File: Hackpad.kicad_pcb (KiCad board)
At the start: 2 copper layers, 99 x 70 mm, 14 parts, among them SW1 SW_Push, SW2 SW_Push, SW3 SW_Push, SW4 SW_Push, SW5 SW_Push, SW6 RotaryEncoder_Switch_MP, U1 XIAO-RP2040-DIP

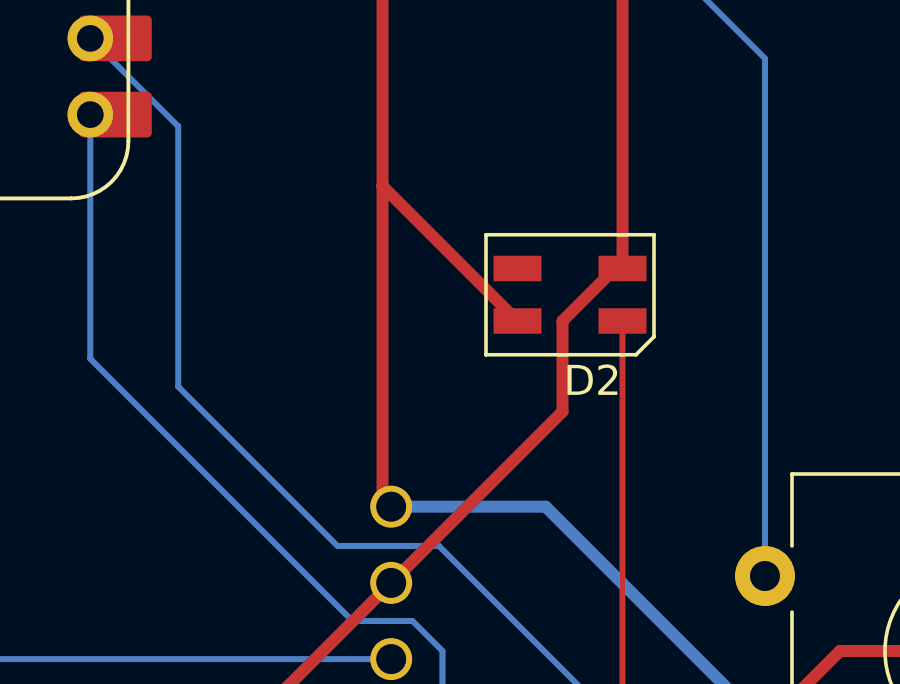
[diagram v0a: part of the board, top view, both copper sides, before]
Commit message: Reroute D2 ground
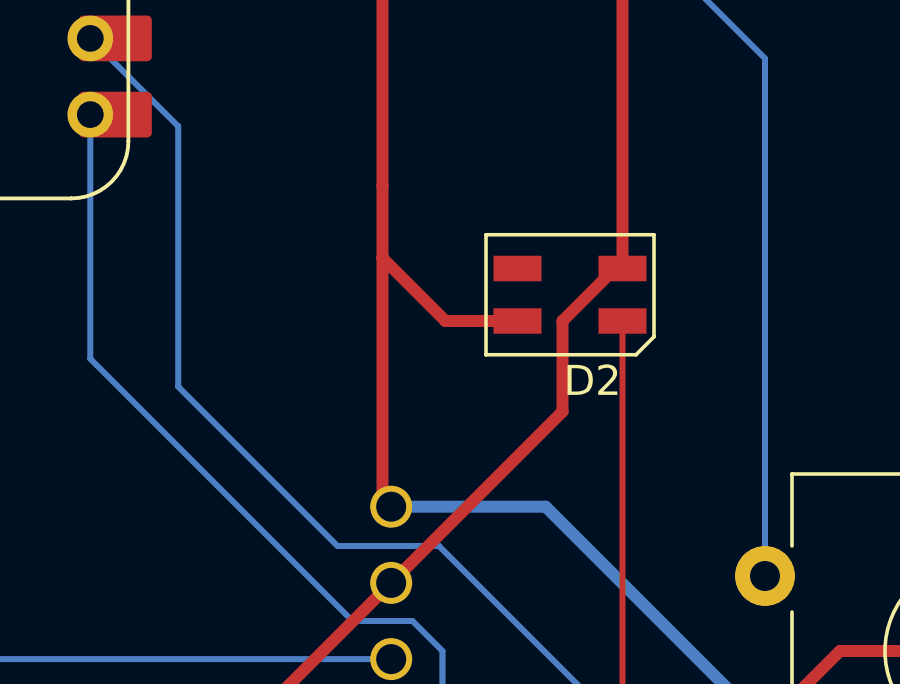
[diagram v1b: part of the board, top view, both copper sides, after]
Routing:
- net GND: track 181.7 -> 180.7 mm
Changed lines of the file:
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@@
+	)
+	(segment
+		(start 134.1 93)
+		(end 132 90.9)
+		(width 0.4)
+		(layer "F.Cu")
+		(net 5)
 	)
 	(segment
@@
 	)
 	(segment
-		(start 132 88.5)
+		(start 132 90.9)
 		(end 132 98.9)
 		(width 0.4)
@@
 		(start 145.415 121.12625)
 		(end 107.315 121.12625)
+		(width 0.4)
+		(layer "F.Cu")
+		(net 5)
+	)
+	(segment
+		(start 136.5 93)
+		(end 134.1 93)
 		(width 0.4)
 		(layer "F.Cu")
@@
 	(segment
 		(start 132 88.5)
-		(end 136.5 93)
+		(end 132 90.9)
 		(width 0.4)
 		(layer "F.Cu")

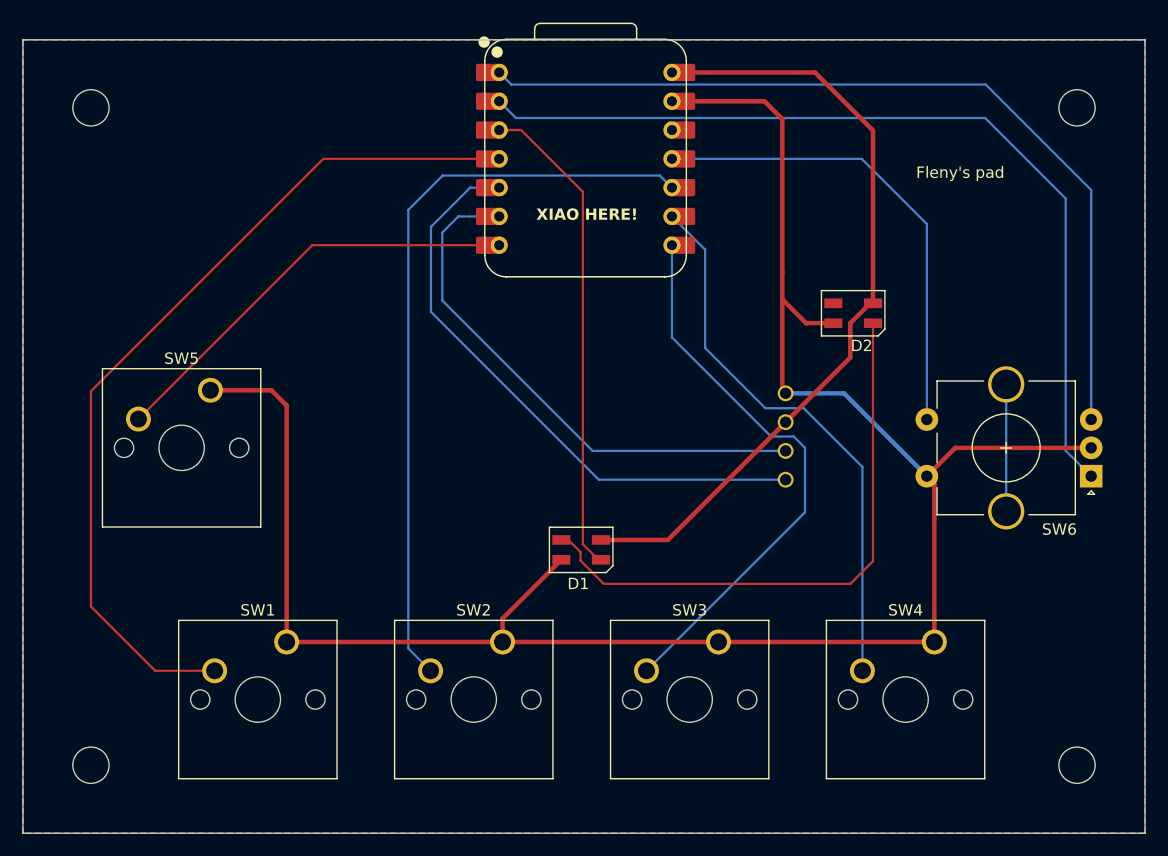
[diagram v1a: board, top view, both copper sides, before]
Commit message: Resize routes
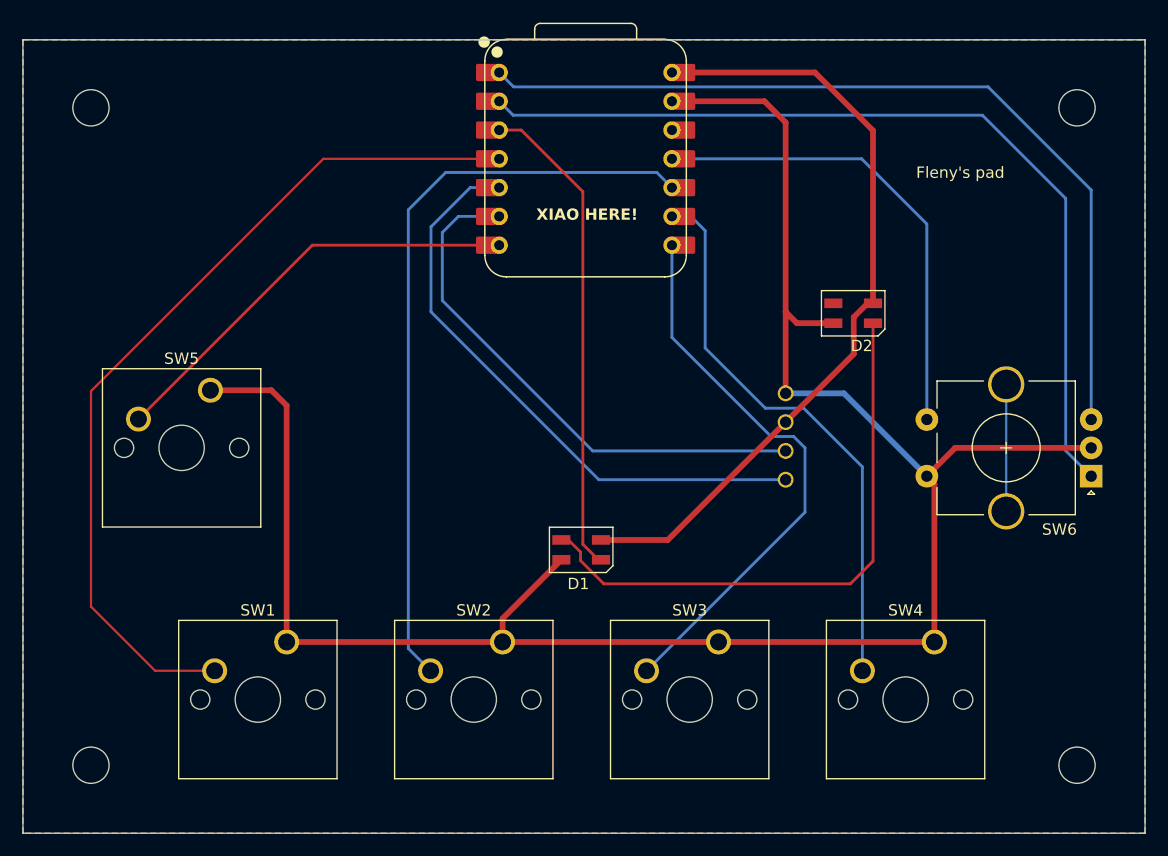
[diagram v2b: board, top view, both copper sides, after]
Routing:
- net Net-(U1-GPIO2/SCK): track 49.0 -> 50.0 mm
- net GND: track 180.7 -> 179.9 mm
- net Net-(D1-DOUT): track 51.4 -> 50.7 mm

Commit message: Rotate oled & reroute
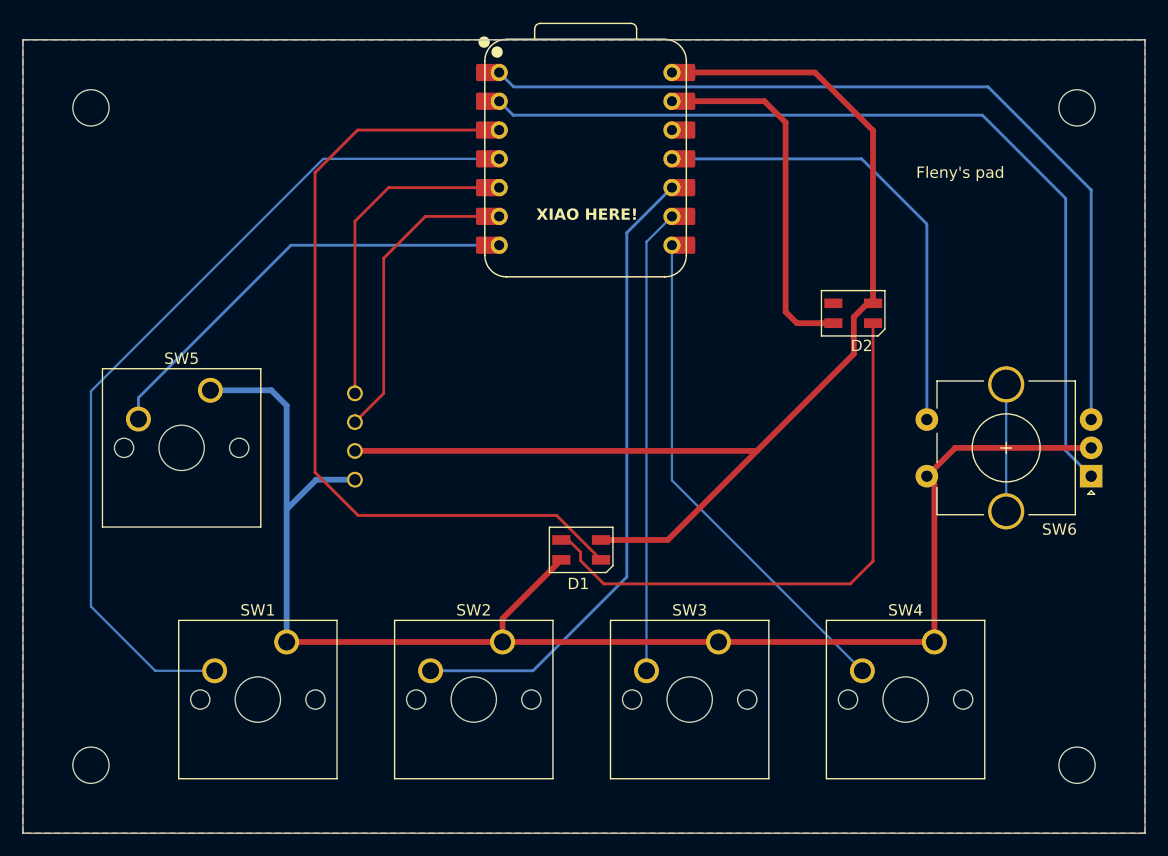
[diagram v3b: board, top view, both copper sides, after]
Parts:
- moved OL1 38.0 mm to (94.3, 103.0), turned to -90 degrees
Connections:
- SW3 pad 2: Net-(U1-GPIO1/RX) -> Net-(U1-GPIO2/SCK)
- SW4 pad 2: Net-(U1-GPIO2/SCK) -> Net-(U1-GPIO1/RX)
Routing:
- net +5V: track 69.2 -> 104.6 mm
- net Net-(D1-DIN): track 42.7 -> 72.7 mm
- net Net-(OL1-SDA): track 52.4 -> 29.1 mm
- net Net-(OL1-SCL): track 47.4 -> 27.2 mm
- net GND: track 179.9 -> 164.4 mm
- net Net-(U1-GPIO4/MISO): track 66.7 -> 56.7 mm
- net Net-(U1-GPIO2/SCK): track 50.0 -> 41.0 mm
- net Net-(U1-GPIO1/RX): track 49.4 -> 44.5 mm
- net Net-(U1-GPIO0/TX): track 38.2 -> 39.3 mm

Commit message: Center oled, SW5 and Rotary
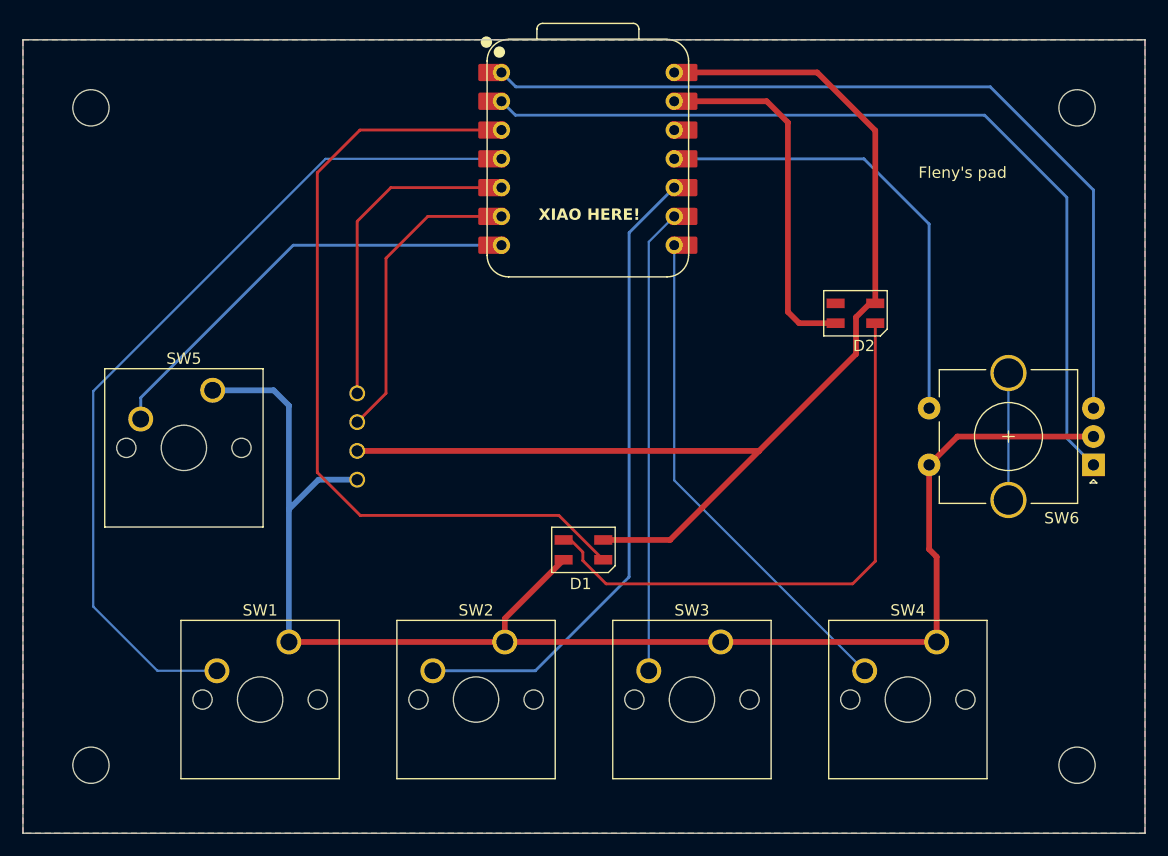
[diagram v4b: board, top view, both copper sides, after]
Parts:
- moved SW6 1.02 mm to (159.4, 105.5)
- moved SW4 0.20 mm to (145.6, 121.1)
- moved D1 0.20 mm to (114.5, 113.0)
- moved SW1 0.20 mm to (88.5, 121.1)
- moved SW2 0.20 mm to (107.5, 121.1)
- moved SW3 0.20 mm to (126.6, 121.1)
- moved U1 0.20 mm to (114.8, 78.5)
- moved D2 0.20 mm to (138.4, 92.1)
- moved OL1 0.20 mm to (94.5, 103.0)
- moved SW5 0.20 mm to (81.7, 98.9)
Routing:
- net GND: track 164.4 -> 165.4 mm
- net Net-(U1-GPIO27/ADC1/A1): track 79.0 -> 78.0 mm
- net Net-(U1-GPIO26/ADC0/A0): track 76.8 -> 75.8 mm
- net Net-(U1-GPIO3/MOSI): track 42.1 -> 41.1 mm

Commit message: Center
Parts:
- moved SW6 2.45 mm to (157.0, 105.5)
- moved OL1 1.26 mm to (95.8, 103.0)
- moved SW5 1.04 mm to (82.0, 97.9)
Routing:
- net GND: track 165.4 -> 167.8 mm
- net Net-(U1-GPIO0/TX): track 39.3 -> 37.5 mm
- net +5V: track 104.6 -> 103.4 mm
- net Net-(U1-GPIO27/ADC1/A1): track 78.0 -> 76.8 mm
- net Net-(U1-GPIO3/MOSI): track 41.1 -> 40.1 mm
- net Net-(U1-GPIO26/ADC0/A0): track 75.8 -> 74.8 mm
- net Net-(OL1-SDA): track 29.1 -> 29.7 mm
- net Net-(OL1-SCL): track 27.2 -> 26.7 mm
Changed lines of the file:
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@@
 	(footprint "Rotary_Encoder:RotaryEncoder_Alps_EC11E-Switch_Vertical_H20mm_CircularMountingHoles"
 		(layer "F.Cu")
-		(at 159.45 105.5 180)
+		(at 157 105.5 180)
 		(descr "Alps rotary encoder, EC12E... with switch, vertical shaft, mounting holes with circular drills, http://www.alps.com/prod/info/E/HTML/Encoder/Incremental/EC11/EC11E15204A3.html")
 		(tags "rotary encoder")
@@
 	(footprint "KBD:OLED"
 		(layer "F.Cu")
-		(at 94.49 103 -90)
+		(at 95.75 103 -90)
 		(descr "Connecteur 6 pins")
 		(tags "CONN DEV")
@@
 	(footprint "Button_Switch_Keyboard:SW_Cherry_MX_1.00u_PCB"
 		(layer "F.Cu")
-		(at 81.74 98.92)
+		(at 82.04 97.92)
 		(descr "Cherry MX keyswitch, 1.00u, PCB mount, http://cherryamericas.com/wp-content/uploads/2014/12/mx_cat.pdf")
 		(tags "Cherry MX keyswitch 1.00u PCB")
@@
 			(keep_text_aligned yes)
 		)
-		(gr_text "99"
+		(gr_text "3897.6378"
 			(at 114.5 141.85 0)
 			(layer "User.4")
@@
 			(keep_text_aligned yes)
 		)
-		(gr_text "70"
+		(gr_text "2755.9055"
 			(at 57.85 103 90)
 			(layer "User.4")
@@
 	)
 	(segment
-		(start 94.49 104.27)
+		(start 95.75 104.27)
 		(end 129.95 104.27)
 		(width 0.508)
@@
 	)
 	(segment
-		(start 94.49 84.01)
-		(end 94.49 99.19)
+		(start 97.46 81.04)
+		(end 94.49 84.01)
 		(width 0.254)
 		(layer "F.Cu")
@@
 	)
 	(segment
-		(start 97.46 81.04)
+		(start 94.49 97.93)
 		(end 94.49 84.01)
 		(width 0.254)
@@
 	)
 	(segment
+		(start 95.75 99.19)
+		(end 94.49 97.93)
+		(width 0.254)
+		(layer "F.Cu")
+		(net 2)
+	)
+	(segment
 		(start 97.03 87.27)
-		(end 97.03 99.19)
+		(end 97.03 100.45)
 		(width 0.254)
 		(layer "F.Cu")
@@
 	)
 	(segment
-		(start 97.03 99.19)
-		(end 94.49 101.73)
+		(start 95.75 101.73)
+		(end 97.03 100.45)
 		(width 0.254)
 		(layer "F.Cu")
@@
 	)
 	(segment
+		(start 145 103)
+		(end 157 103)
+		(width 0.508)
+		(layer "F.Cu")
+		(net 5)
+	)
+	(segment
 		(start 133.49 93)
 		(end 132.49 92)
@@
 	)
 	(segment
-		(start 145.615 121.12625)
-		(end 107.515 121.12625)
+		(start 142.5 105.5)
+		(end 145 103)
 		(width 0.508)
 		(layer "F.Cu")
@@
 	)
 	(segment
-		(start 147.45 103)
-		(end 159.45 103)
-		(width 0.508)
-		(layer "F.Cu")
-		(net 5)
-	)
-	(segment
-		(start 145.615 113.615)
-		(end 144.95 112.95)
-		(width 0.508)
-		(layer "F.Cu")
-		(net 5)
-	)
-	(segment
-		(start 144.95 112.95)
-		(end 144.95 105.5)
+		(start 145.615 121.12625)
+		(end 107.515 121.12625)
 		(width 0.508)
 		(layer "F.Cu")
@@
 	)
 	(segment
-		(start 145.615 121.12625)
-		(end 145.615 113.615)
+		(start 145.615 108.615)
+		(end 142.5 105.5)
 		(width 0.508)
 		(layer "F.Cu")
@@
 	)
 	(segment
-		(start 144.95 105.5)
-		(end 147.45 103)
+		(start 136.7 93)
+		(end 133.49 93)
 		(width 0.508)
 		(layer "F.Cu")
@@
 	)
 	(segment
-		(start 136.7 93)
-		(end 133.49 93)
+		(start 145.615 121.12625)
+		(end 145.615 108.615)
 		(width 0.508)
 		(layer "F.Cu")
@@
 	(segment
 		(start 91.075 106.81)
-		(end 88.465 109.42)
+		(end 95.75 106.81)
 		(width 0.508)
 		(layer "B.Cu")
@@
 	(segment
 		(start 88.465 109.42)
-		(end 88.465 121.12625)
+		(end 88.465 100.265)
 		(width 0.508)
 		(layer "B.Cu")
@@
 	)
 	(segment
-		(start 81.74 98.92)
-		(end 87.12 98.92)
+		(start 86.12 97.92)
+		(end 82.04 97.92)
 		(width 0.508)
 		(layer "B.Cu")
@@
 	)
 	(segment
-		(start 88.465 100.265)
-		(end 88.465 109.42)
+		(start 88.465 109.42)
+		(end 91.075 106.81)
 		(width 0.508)
 		(layer "B.Cu")
@@
 	)
 	(segment
-		(start 94.49 106.81)
-		(end 91.075 106.81)
+		(start 88.465 109.42)
+		(end 88.465 121.12625)
 		(width 0.508)
 		(layer "B.Cu")
@@
 	)
 	(segment
-		(start 87.12 98.92)
-		(end 88.465 100.265)
+		(start 88.465 100.265)
+		(end 86.12 97.92)
 		(width 0.508)
 		(layer "B.Cu")
@@
 	)
 	(segment
-		(start 107.22 86.12)
-		(end 88.85 86.12)
+		(start 90.03 86.12)
+		(end 107.22 86.12)
 		(width 0.254)
 		(layer "B.Cu")
@@
 	)
 	(segment
-		(start 75.39 99.58)
-		(end 75.39 101.46)
+		(start 75.69 100.46)
+		(end 90.03 86.12)
 		(width 0.254)
 		(layer "B.Cu")
@@
 	)
 	(segment
-		(start 88.85 86.12)
-		(end 75.39 99.58)
+		(start 149.5 97.4)
+		(end 149.5 108.6)
 		(width 0.254)
 		(layer "B.Cu")
-		(net 8)
-	)
-	(segment
-		(start 151.95 98.4)
-		(end 151.95 109.6)
-		(width 0.2)
-		(layer "B.Cu")
 		(net 9)
 	)
@@
 	)
 	(segment
-		(start 159.45 81.25)
-		(end 150.35 72.15)
+		(start 157 100.5)
+		(end 157 78.8)
 		(width 0.254)
 		(layer "B.Cu")
@@
 	)
 	(segment
-		(start 159.45 81.25)
-		(end 159.45 100.5)
+		(start 157 78.8)
+		(end 150.35 72.15)
 		(width 0.254)
 		(layer "B.Cu")
@@
 	)
 	(segment
-		(start 157.1 81.9)
-		(end 149.85 74.65)
+		(start 154.28 103.12)
+		(end 154.28 79.08)
 		(width 0.254)
 		(layer "B.Cu")
@@
 	)
 	(segment
-		(start 108.45 74.65)
-		(end 107.22 73.42)
+		(start 156.66 105.5)
+		(end 154.28 103.12)
 		(width 0.254)
 		(layer "B.Cu")
@@
 	)
 	(segment
-		(start 157.1 81.9)
-		(end 157.1 103.15)
+		(start 154.28 79.08)
+		(end 149.85 74.65)
 		(width 0.254)
 		(layer "B.Cu")
@@
 	)
 	(segment
-		(start 149.85 74.65)
-		(end 108.45 74.65)
+		(start 108.45 74.65)
+		(end 107.22 73.42)
 		(width 0.254)
 		(layer "B.Cu")
@@
 	)
 	(segment
-		(start 157.1 103.15)
-		(end 159.45 105.5)
+		(start 149.85 74.65)
+		(end 108.45 74.65)
 		(width 0.254)
 		(layer "B.Cu")
@@
 	)
 	(segment
-		(start 144.95 84.25)
-		(end 144.95 100.5)
+		(start 142.5 81.8)
+		(end 139.2 78.5)
 		(width 0.254)
 		(layer "B.Cu")
@@
 	(segment
 		(start 139.2 78.5)
-		(end 144.95 84.25)
+		(end 122.46 78.5)
 		(width 0.254)
 		(layer "B.Cu")
@@
 	)
 	(segment
-		(start 122.46 78.5)
-		(end 139.2 78.5)
+		(start 142.5 100.5)
+		(end 142.5 81.8)
 		(width 0.254)
 		(layer "B.Cu")
